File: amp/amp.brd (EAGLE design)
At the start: 99.1 x 80 mm, 71 parts, among them IC1 OPA2134PA, Q1 BC547, Q10 IRF540, Q11 BC556, Q12 BC556, Q13 BC547, Q14 BC547, Q15 2N7000, Q16 BC547, Q17 BC547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

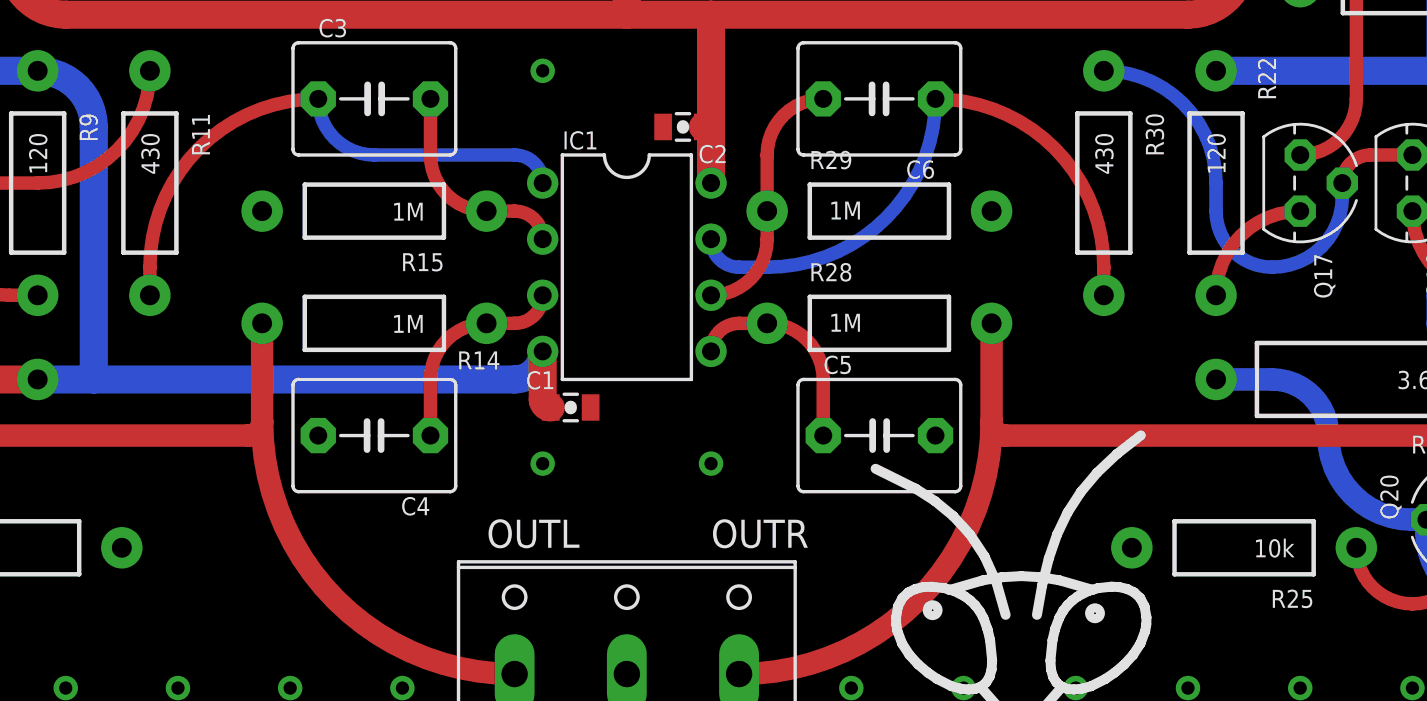
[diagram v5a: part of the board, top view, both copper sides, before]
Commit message: HT filter added
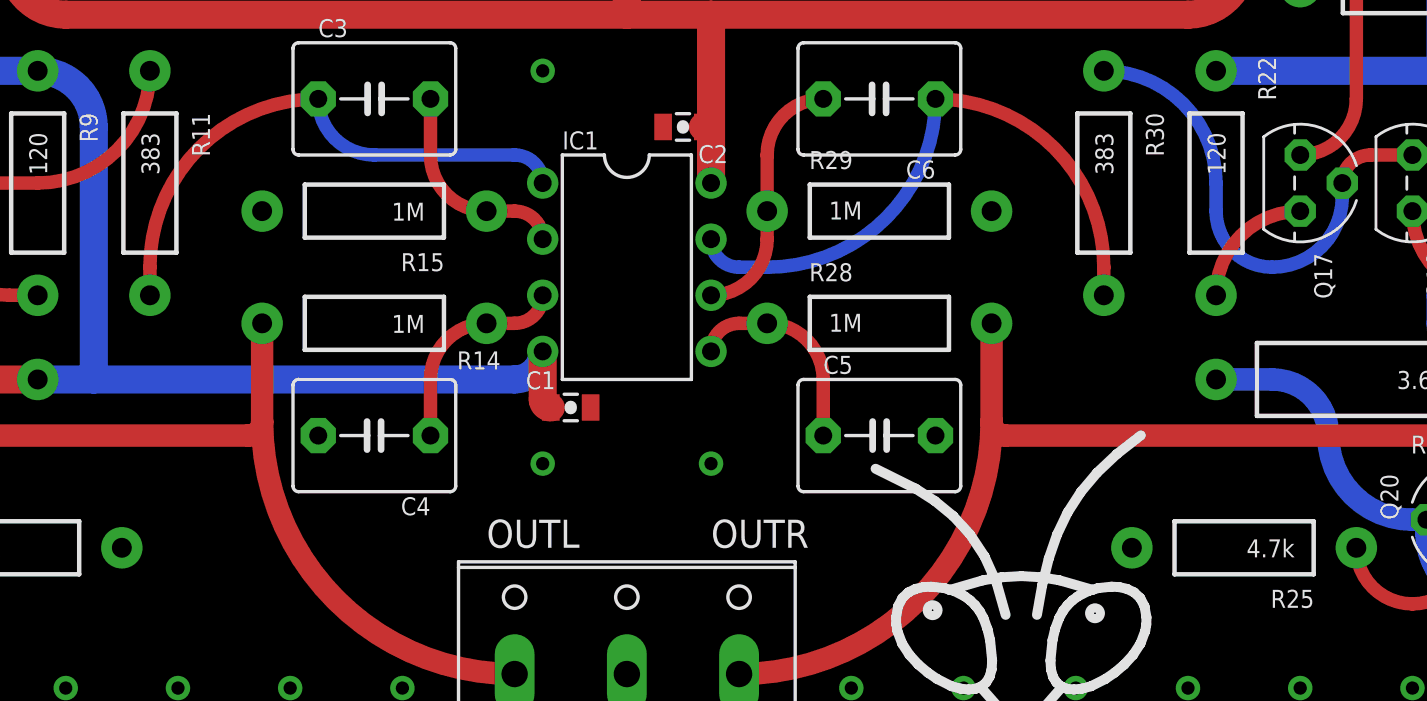
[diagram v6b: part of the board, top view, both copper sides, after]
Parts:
- Q16, Q17, Q6, Q7: value BC547 -> BC337; device transistor-npn:TO92 -> transistor:TO92
- R11, R30: value 430 -> 383
- R25: value 10k -> 4.7k
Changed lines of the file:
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@@
 </element>
 <element name="R8" library="SparkFun-Resistors" package="AXIAL-0.4" value="2.2k" x="13.97" y="41.91"/>
-<element name="Q7" library="transistor-npn" package="TO92" value="BC547" x="12.7" y="26.67" smashed="yes" rot="R270">
+<element name="Q7" library="transistor" package="TO92" value="BC337" x="12.7" y="26.67" smashed="yes" rot="R270">
 <attribute name="NAME" x="13.335" y="23.495" size="0.8128" layer="25" ratio="15" rot="R270"/>
 <attribute name="VALUE" x="11.43" y="23.495" size="0.8128" layer="27" ratio="15" rot="R270"/>
 </element>
-<element name="Q6" library="transistor-npn" package="TO92" value="BC547" x="17.78" y="26.67" smashed="yes" rot="R270">
+<element name="Q6" library="transistor" package="TO92" value="BC337" x="17.78" y="26.67" smashed="yes" rot="R270">
 <attribute name="NAME" x="18.415" y="23.495" size="0.8128" layer="25" ratio="15" rot="R270"/>
 <attribute name="VALUE" x="16.51" y="23.495" size="0.8128" layer="27" ratio="15" rot="R270"/>
@@
 <attribute name="VALUE" x="35.56" y="28.194" size="0.8128" layer="27" ratio="15"/>
 </element>
-<element name="R11" library="SparkFun-Resistors" package="AXIAL-0.4" value="430" x="27.94" y="26.67" rot="R270"/>
+<element name="R11" library="SparkFun-Resistors" package="AXIAL-0.4" value="383" x="27.94" y="26.67" rot="R270"/>
 <element name="C1" library="SparkFun-Capacitors" package="0805-CAP" value="1.0uF" x="46.99" y="16.51" smashed="yes">
 <attribute name="PROD_ID" value="CAP-11625" x="46.99" y="16.51" size="1.778" layer="27" display="off"/>
@@
 </element>
 <element name="R21" library="SparkFun-Resistors" package="AXIAL-0.4" value="2.2k" x="85.09" y="41.91" rot="R180"/>
-<element name="Q16" library="transistor-npn" package="TO92" value="BC547" x="85.09" y="26.67" smashed="yes" rot="R270">
+<element name="Q16" library="transistor" package="TO92" value="BC337" x="85.09" y="26.67" smashed="yes" rot="R270">
 <attribute name="NAME" x="85.725" y="23.495" size="0.8128" layer="25" ratio="15" rot="R270"/>
 <attribute name="VALUE" x="83.82" y="23.495" size="0.8128" layer="27" ratio="15" rot="R270"/>
 </element>
-<element name="Q17" library="transistor-npn" package="TO92" value="BC547" x="80.01" y="26.67" smashed="yes" rot="R270">
+<element name="Q17" library="transistor" package="TO92" value="BC337" x="80.01" y="26.67" smashed="yes" rot="R270">
 <attribute name="NAME" x="80.645" y="23.495" size="0.8128" layer="25" ratio="15" rot="R270"/>
 <attribute name="VALUE" x="78.74" y="23.495" size="0.8128" layer="27" ratio="15" rot="R270"/>
@@
 <attribute name="VALUE" x="85.979" y="18.161" size="0.8128" layer="21" font="vector" ratio="15" rot="R180"/>
 </element>
-<element name="R25" library="SparkFun-Resistors" package="AXIAL-0.4" value="10k" x="77.47" y="10.16" rot="R180"/>
+<element name="R25" library="SparkFun-Resistors" package="AXIAL-0.4" value="4.7k" x="77.47" y="10.16" rot="R180"/>
 <element name="R26" library="SparkFun-Resistors" package="AXIAL-0.4" value="10k" x="85.09" y="35.56" rot="R180"/>
 <element name="R27" library="SparkFun-Resistors" package="AXIAL-0.4" value="2K" x="71.12" y="41.91"/>
@@
 <attribute name="VALUE" x="63.5" y="32.766" size="0.8128" layer="27" ratio="15" rot="R180"/>
 </element>
-<element name="R30" library="SparkFun-Resistors" package="AXIAL-0.4" value="430" x="71.12" y="26.67" rot="R270"/>
+<element name="R30" library="SparkFun-Resistors" package="AXIAL-0.4" value="383" x="71.12" y="26.67" rot="R270"/>
 <element name="LOGO1" library="my" package="LOGO-MANTIS" value="LOGO-MANTIS" x="67.31" y="8.89"/>
 <element name="R31" library="SparkFun-Electromechanical" package="3362U-2" value="500" x="10.16" y="71.12" smashed="yes"/>

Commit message: More tweaks
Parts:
- R13, R24: value 3.6 -> 2.4
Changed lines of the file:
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@@
 <attribute name="VALUE" x="15.875" y="11.43" size="0.8128" layer="27" ratio="15" rot="R90"/>
 </element>
-<element name="R13" library="SparkFun-Resistors" package="AXIAL-0.5" value="3.6" x="16.51" y="17.78" smashed="yes" rot="R180">
+<element name="R13" library="SparkFun-Resistors" package="AXIAL-0.5" value="2.4" x="16.51" y="17.78" smashed="yes" rot="R180">
 <attribute name="NAME" x="20.955" y="15.24" size="0.8128" layer="25" font="vector" ratio="15" rot="R180"/>
 <attribute name="VALUE" x="19.939" y="18.161" size="0.8128" layer="21" font="vector" ratio="15" rot="R180"/>
@@
 <attribute name="VALUE" x="90.805" y="10.16" size="0.8128" layer="27" ratio="15" rot="R90"/>
 </element>
-<element name="R24" library="SparkFun-Resistors" package="AXIAL-0.5" value="3.6" x="82.55" y="17.78" smashed="yes" rot="R180">
+<element name="R24" library="SparkFun-Resistors" package="AXIAL-0.5" value="2.4" x="82.55" y="17.78" smashed="yes" rot="R180">
 <attribute name="NAME" x="86.995" y="15.24" size="0.8128" layer="25" font="vector" ratio="15" rot="R180"/>
 <attribute name="VALUE" x="85.979" y="18.161" size="0.8128" layer="21" font="vector" ratio="15" rot="R180"/>

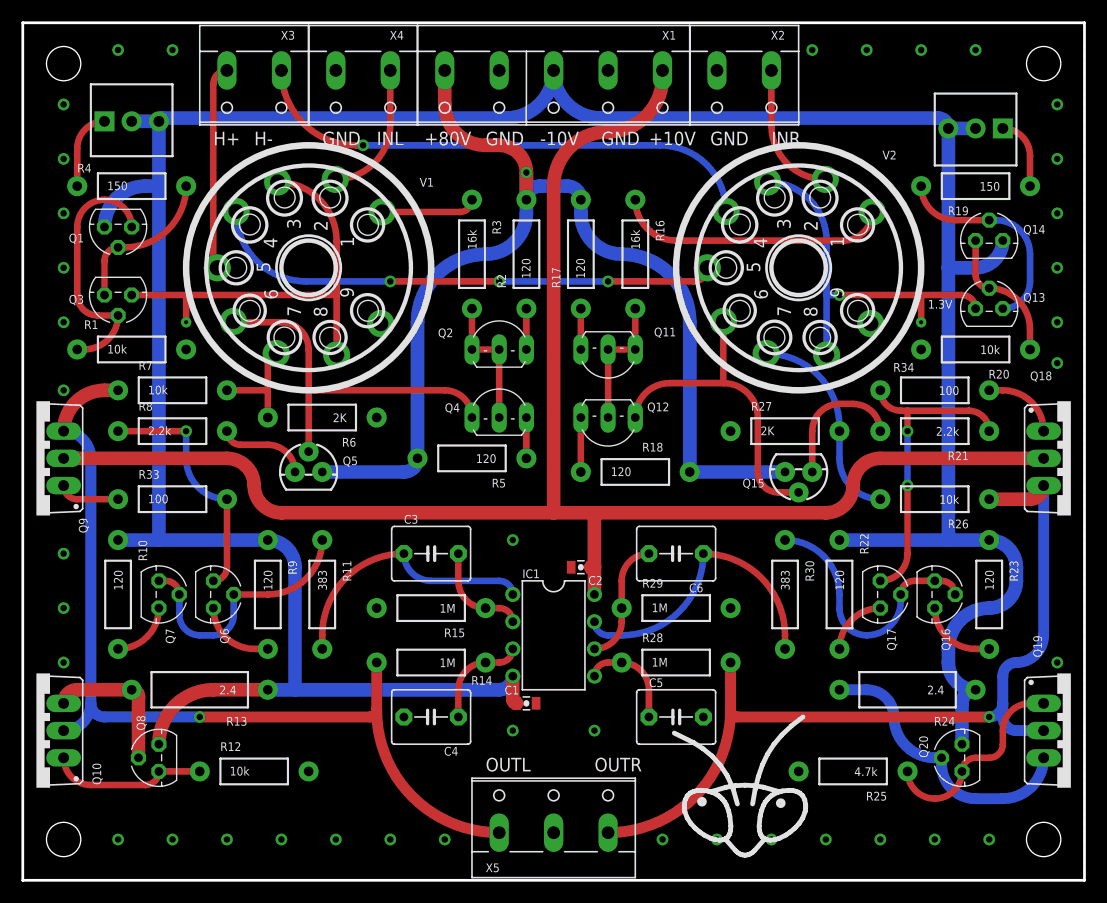
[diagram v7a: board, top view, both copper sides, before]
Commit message: Small bypass cap added
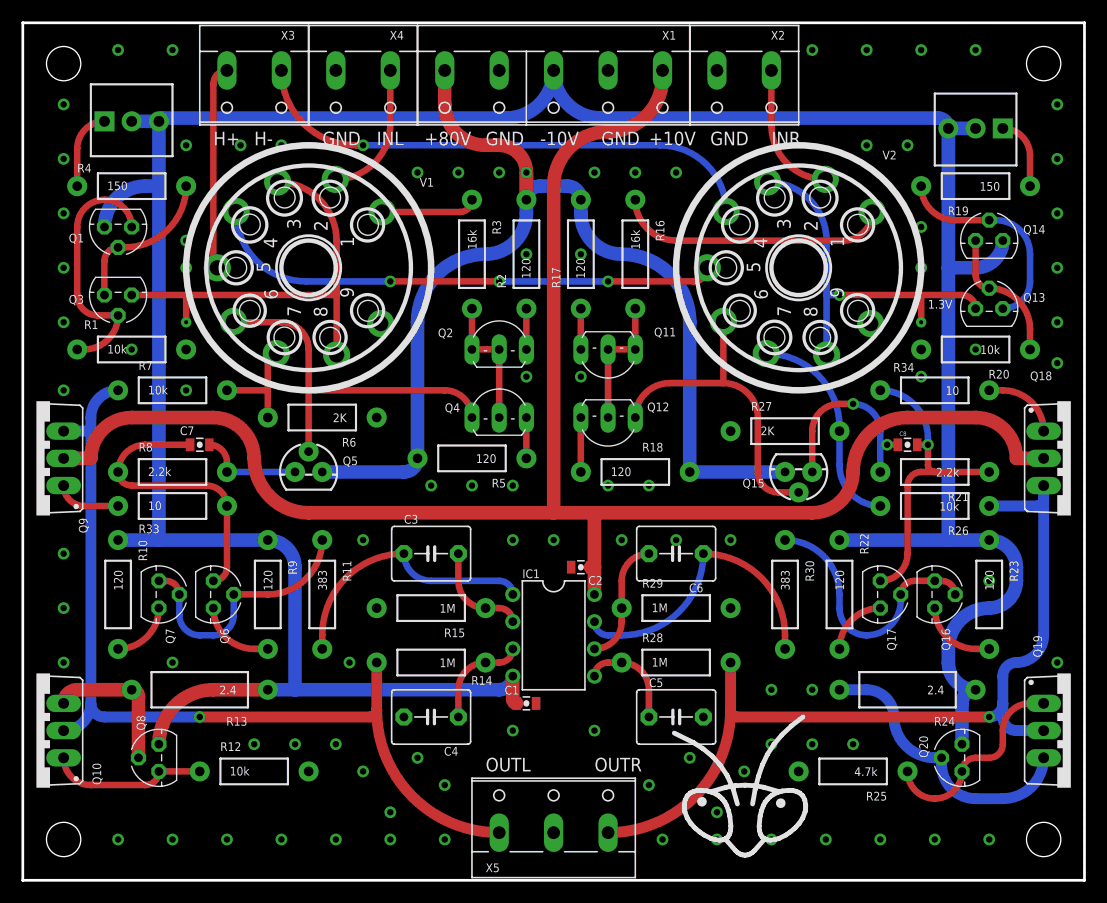
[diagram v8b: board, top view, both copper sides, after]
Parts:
- added C7, C8: 82nF, SparkFun-Capacitors:0805-CAP
- R33, R34: value 100 -> 10
- moved R21 3.81 mm to (85.1, 38.1)
- moved R8 3.81 mm to (14.0, 38.1)
- moved R26 0.64 mm to (85.1, 34.9)
- moved R33 0.64 mm to (14.0, 34.9)
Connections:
- net N$13: now also C7.2
- net N$14: now also C7.1
- net N$31: now also C8.2
- net N$32: now also C8.1
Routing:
- net VCC: track 149.1 -> 155.4 mm
- net N$32: track 12.3 -> 17.7 mm, vias 0 -> 2
- net N$13: track 22.4 -> 26.8 mm, vias 1 -> 0
- net N$14: track 7.93 -> 9.57 mm
- net N$35: track 18.0 -> 18.6 mm
- net N$31: track 28.7 -> 28.8 mm, vias 2 -> 1
